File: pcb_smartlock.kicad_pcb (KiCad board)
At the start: 2 copper layers, 36.7 x 36.7 mm, 55 parts, among them IC1 ST25R3918-AQET, J1 Conn_01x02, J2 Conn_01x03, Q3 IRLML6344TRPBF, Q4 IRLML6344TRPBF, U2 SPX3819M5-L-1-8, U3 ESP32-C3-MINI-1-H4X, U5 SPX3819M5-L-1-8

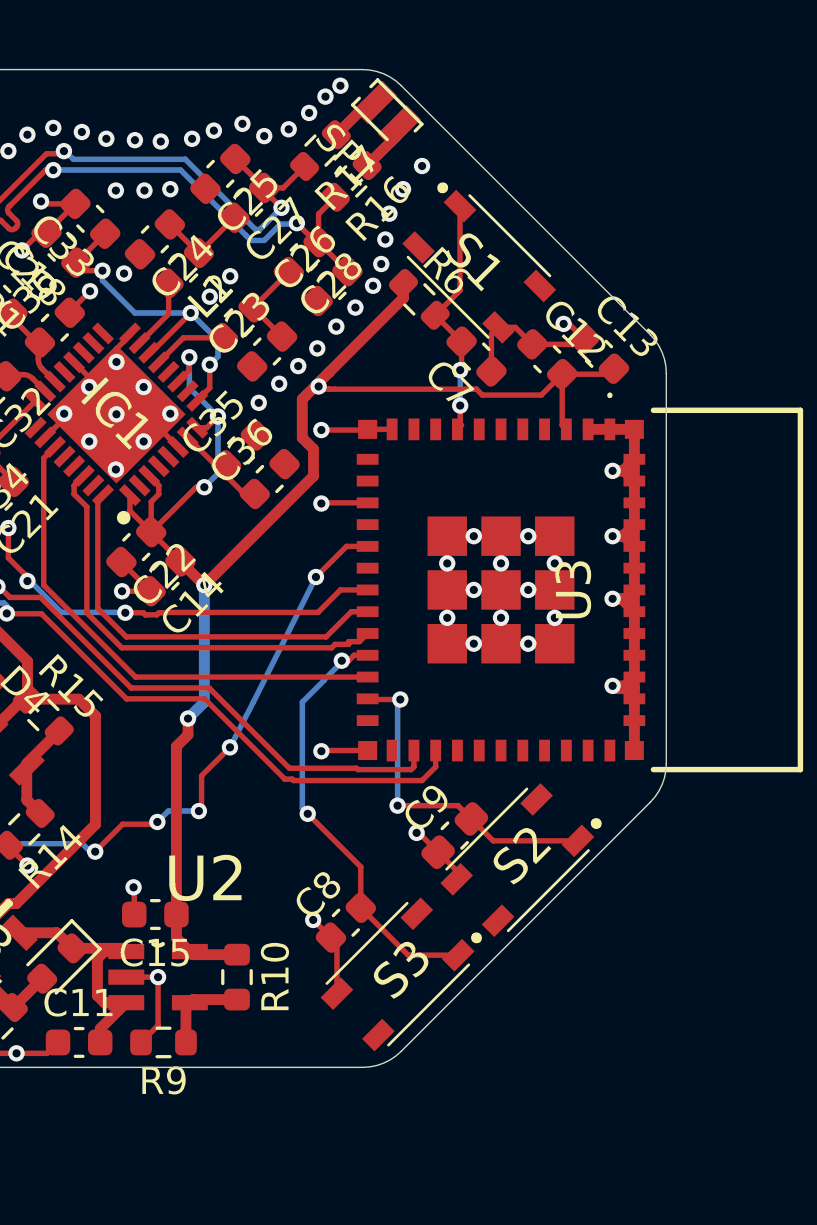
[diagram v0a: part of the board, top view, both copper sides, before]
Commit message: Finition PCB des boutons
J'ai relié chacun des 3 boutons à leur source de tension et à un GND.
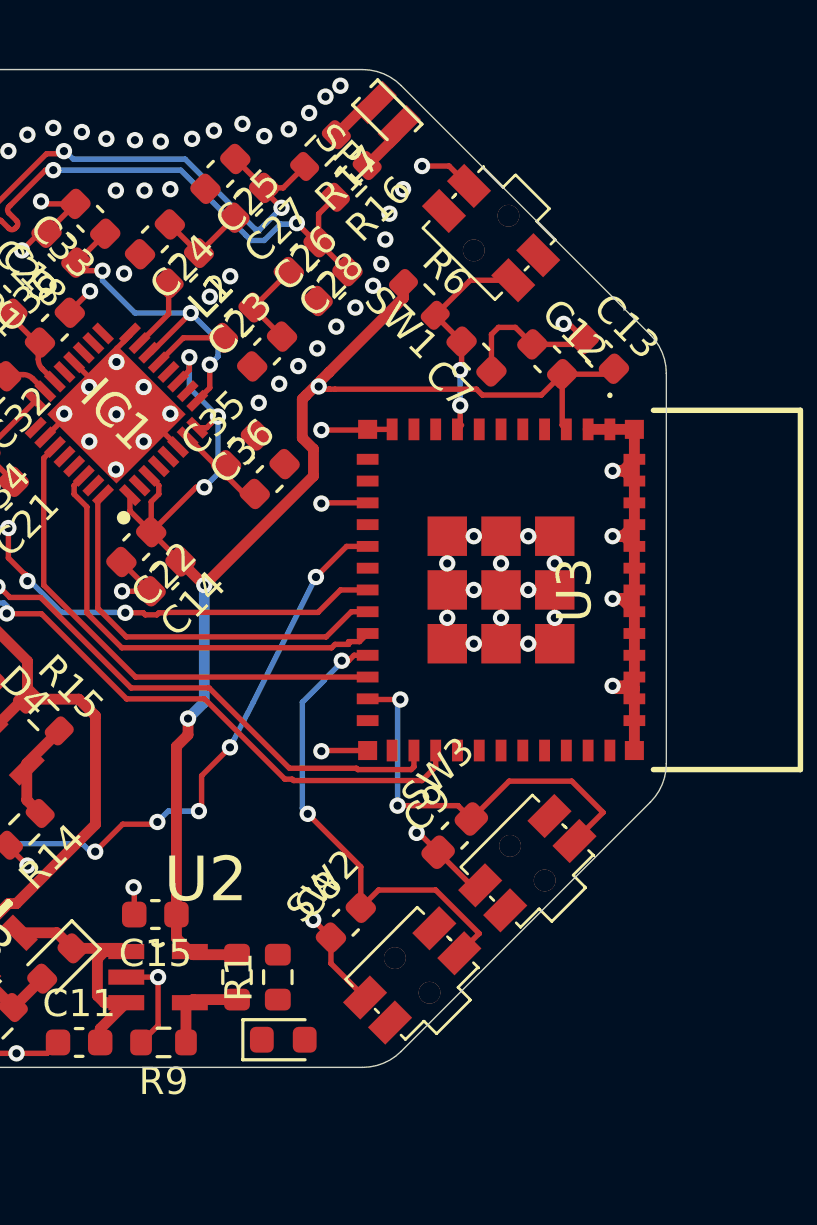
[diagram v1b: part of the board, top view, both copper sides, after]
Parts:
- removed S1, S2, S3: PTS810SJM250SMTRLFS, PTS810SJM250SMTRLFS:PTS810SJG250SMTRLFS
- added D1: LED, LED_SMD:LED_0603_1608Metric, F.Cu at (129.5, 111.5)
- added R1: 10k, Resistor_SMD:R_0603_1608Metric, F.Cu at (129.3, 109.2)
- added SW1: SKSCLBE010, SKSCLBE010:KEY-SMD_4P-SKSCLXX010, F.Cu at (137.1, 81.9)
- added SW2: SKSCLBE010, SKSCLBE010:KEY-SMD_4P-SKSCLXX010, F.Cu at (134.2, 109.1)
- added SW3: SKSCLBE010, SKSCLBE010:KEY-SMD_4P-SKSCLXX010, F.Cu at (138.5, 105.0)
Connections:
- U3 pad 13: unconnected-(U3-IO1-Pad13) -> GPIO-LED
- USBC1 pad A9: unconnected-(USBC1-VBUS-PadA9) -> Net-(D5-A)
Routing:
- net GND: track 103.3 -> 107.0 mm
- net Boot_Button: track 12.3 -> 15.4 mm
- net Sync_button: track 15.9 -> 17.9 mm
- net Reset_Button: track 9.26 -> 8.27 mm

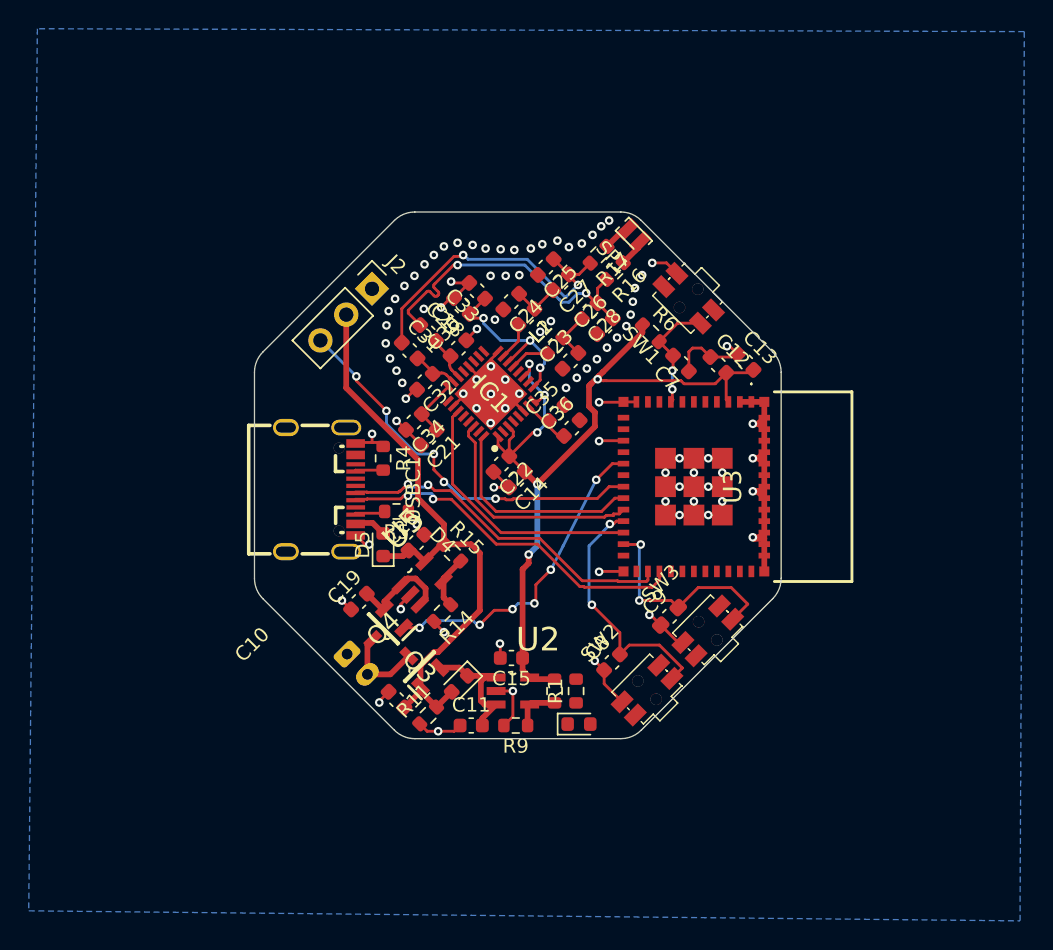
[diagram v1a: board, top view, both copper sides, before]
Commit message: Fix most of routing
TODO : silkscreen
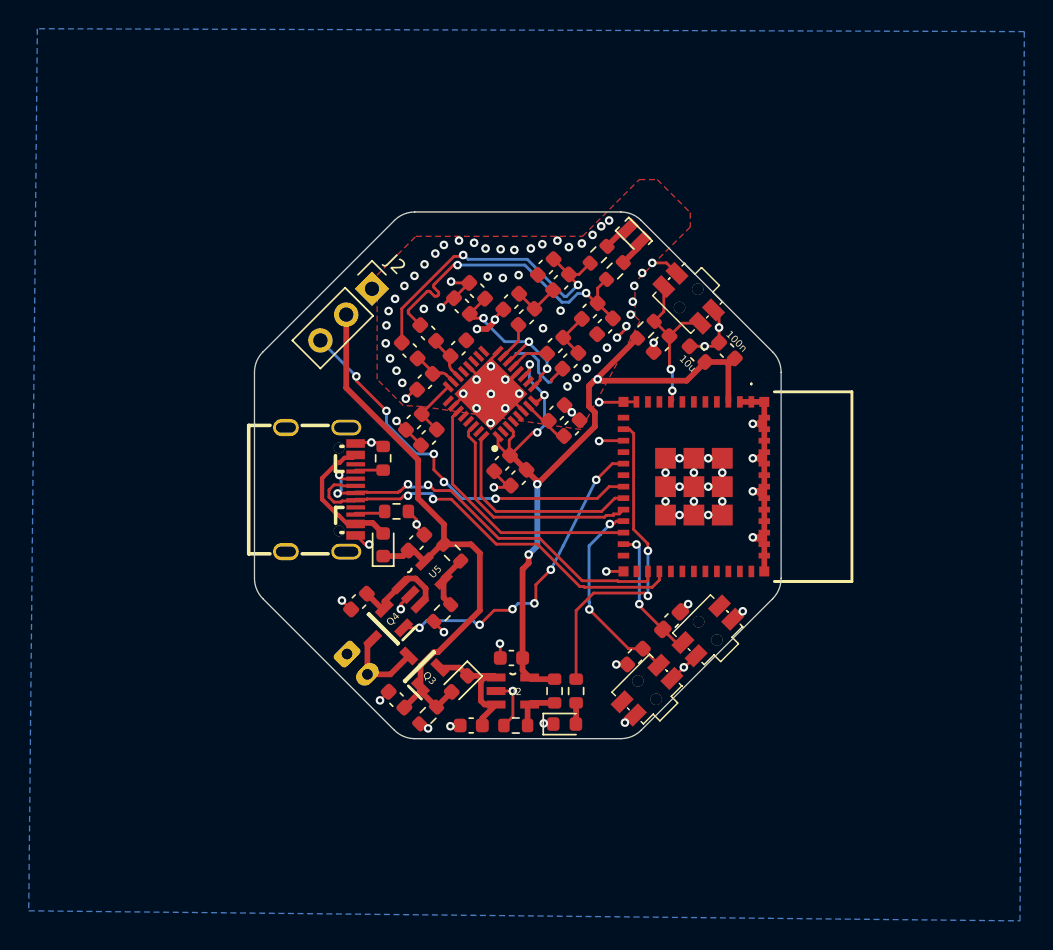
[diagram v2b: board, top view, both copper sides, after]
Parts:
- R4: value 5.1k -> 5.1K
- R5: value 5.1K -> 5.1k
- moved C7 1.91 mm to (135.2, 85.0), turned to 45 degrees
- moved C8 1.65 mm to (133.4, 106.8)
- moved C12 1.63 mm to (137.8, 85.8)
- moved C13 1.53 mm to (139.8, 85.5)
- moved D1 1.00 mm to (128.5, 111.5)
- moved R6 0.43 mm to (134.2, 84.0), turned to 45 degrees
- moved C9 0.34 mm to (135.9, 104.3), turned to -135 degrees
- moved C14 0.18 mm to (125.3, 94.3)
- moved C22 0.07 mm to (124.2, 93.3)
- turned R4 to 90 degrees
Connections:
- R4 pad 1: GND -> Net-(USBC1-CC1)
- R4 pad 2: Net-(USBC1-CC2) -> GND
- R5 pad 1: Net-(USBC1-CC1) -> GND
- R5 pad 2: GND -> Net-(USBC1-CC2)
- SW2 pad 1: Sync_button -> GND
- SW2 pad 2: Sync_button -> GND
- SW2 pad 3: GND -> Sync_button
- SW2 pad 4: GND -> Sync_button
- SW3 pad 1: Boot_Button -> GND
- SW3 pad 2: Boot_Button -> GND
- SW3 pad 3: GND -> Boot_Button
- SW3 pad 4: GND -> Boot_Button
- U3 pad 13: GPIO-LED -> GPIO_LED
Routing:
- net GPIO_LED: track 0.00 -> 23.1 mm, vias 0 -> 2
- net Net-(D5-A): track 2.20 -> 9.72 mm
- net Boot_Button: track 15.4 -> 9.42 mm
- net D+: track 25.0 -> 29.6 mm
- net D-: track 24.2 -> 28.3 mm, vias 2 -> 4
- net Sync_button: track 17.9 -> 14.1 mm
- net Reset_Button: track 8.27 -> 11.8 mm
- net GND: track 107.0 -> 103.7 mm, vias 91 -> 99
- net Net-(USBC1-CC1): track 0.00 -> 1.96 mm
- net +3.3V: track 61.4 -> 59.9 mm
- net Net-(D1-A): track 0.00 -> 1.48 mm
- added copper zone on F.Cu, net GND
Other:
- board text added: "100n"
- board text added: "10u"
